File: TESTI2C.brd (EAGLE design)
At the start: 53.3 x 53.3 mm, 20 parts, among them J1 Digital_0_7, J2 Analog, J3 Digital_8_13

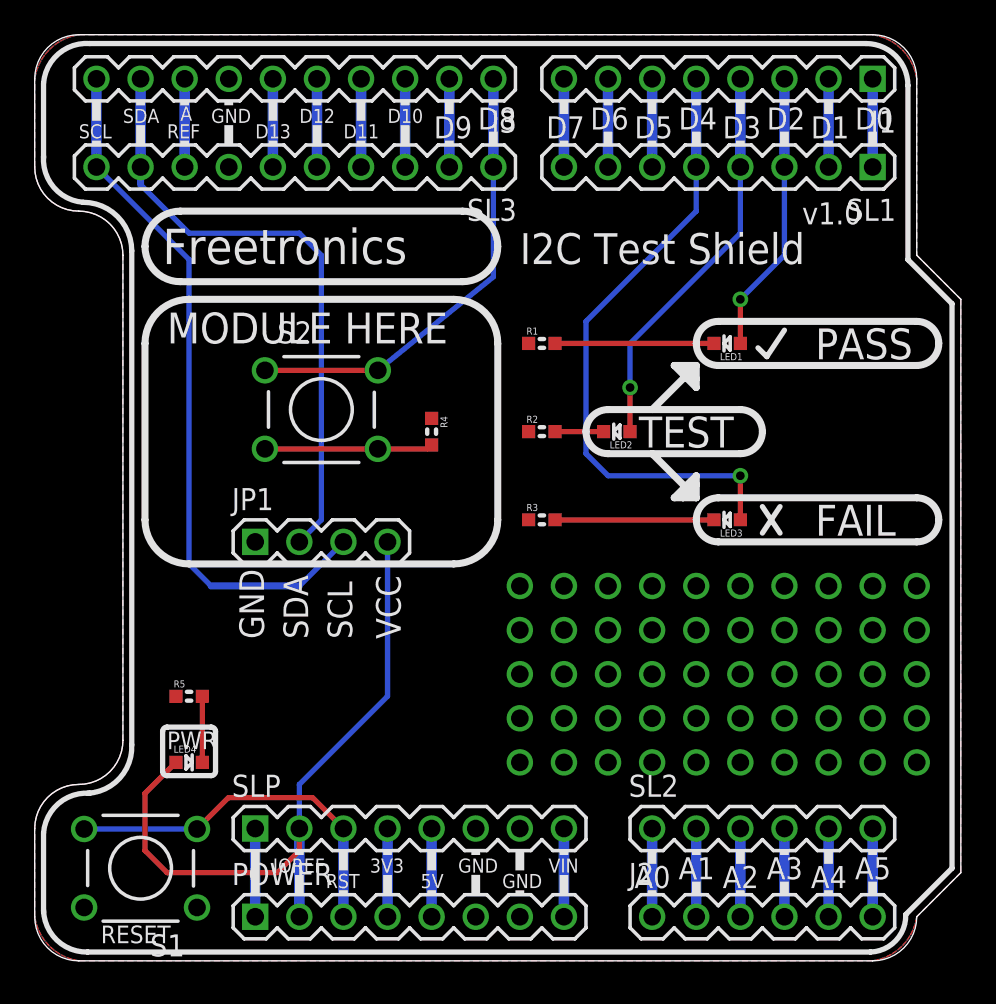
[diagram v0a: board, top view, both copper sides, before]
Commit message: Added piezo
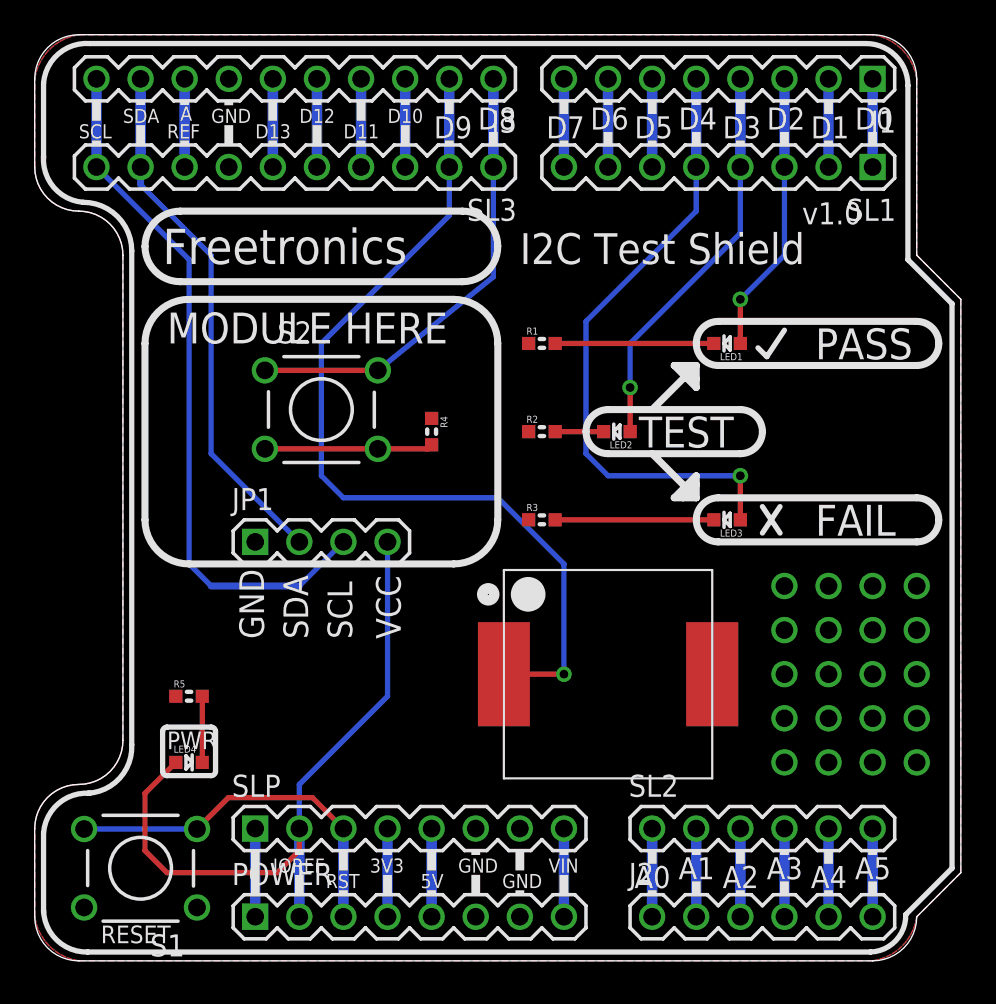
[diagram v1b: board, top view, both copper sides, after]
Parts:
- added PIEZO: BUZZERSMD12X12, freetronics-master-v1:BUZZER-12X12-SMT
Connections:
- net D9: now also PIEZO.2
- net GND: now also PIEZO.1
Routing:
- net D9: track 5.08 -> 51.8 mm, vias 0 -> 1
- net SDA: track 35.2 -> 30.5 mm
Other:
- board text added: "D2: PASS D3: TEST D4: FAIL D8: nDETECT D9: PIEZO"
- board text removed: "D2: PASS D3: TEST D4: FAIL D8: nDETECT"
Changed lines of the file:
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@@
 D3: TEST
 D4: FAIL
-D8: nDETECT</text>
+D8: nDETECT
+D9: PIEZO</text>
 <text x="7.62" y="12.192" size="1.016" layer="21" ratio="15">PWR</text>
 <wire x1="7.62" y1="13.462" x2="7.366" y2="13.208" width="0.3048" layer="21" curve="90"/>
@@
 <element name="LED4" library="freetronics-jon" package="LED-0603" value="BLUE" x="8.89" y="11.43"/>
 <element name="R5" library="freetronics-jon" package="0603" value="1K5 0603" x="8.89" y="15.24"/>
+<element name="PIEZO" library="freetronics-master-v1" package="BUZZER-12X12-SMT" value="BUZZERSMD12X12" x="33.02" y="16.51" rot="R180"/>
 </elements>
 <signals>
@@
 <contactref element="J3" pad="2"/>
 <wire x1="23.876" y1="45.72" x2="23.876" y2="50.8" width="0.6096" layer="16"/>
+<contactref element="PIEZO" pad="2"/>
+<wire x1="27.02" y1="16.51" x2="30.48" y2="16.51" width="0.3048" layer="1"/>
+<via x="30.48" y="16.51" extent="1-16" drill="0.5"/>
+<wire x1="30.48" y1="16.51" x2="30.48" y2="22.86" width="0.3048" layer="16"/>
+<wire x1="30.48" y1="22.86" x2="26.67" y2="26.67" width="0.3048" layer="16"/>
+<wire x1="26.67" y1="26.67" x2="17.78" y2="26.67" width="0.3048" layer="16"/>
+<wire x1="17.78" y1="26.67" x2="16.51" y2="27.94" width="0.3048" layer="16"/>
+<wire x1="16.51" y1="27.94" x2="16.51" y2="35.56" width="0.3048" layer="16"/>
+<wire x1="16.51" y1="35.56" x2="23.876" y2="42.926" width="0.3048" layer="16"/>
+<wire x1="23.876" y1="42.926" x2="23.876" y2="45.72" width="0.3048" layer="16"/>
 </signal>
 <signal name="D8">
@@
 <contactref element="JP1" pad="1"/>
 <contactref element="R5" pad="1"/>
+<contactref element="PIEZO" pad="1"/>
 </signal>
 <signal name="SDA">
@@
 <wire x1="6.096" y1="50.8" x2="6.096" y2="45.72" width="0.6096" layer="16"/>
 <contactref element="JP1" pad="2"/>
-<wire x1="15.24" y1="24.13" x2="16.51" y2="25.4" width="0.3048" layer="16"/>
-<wire x1="16.51" y1="25.4" x2="16.51" y2="40.64" width="0.3048" layer="16"/>
-<wire x1="16.51" y1="40.64" x2="15.24" y2="41.91" width="0.3048" layer="16"/>
-<wire x1="15.24" y1="41.91" x2="8.89" y2="41.91" width="0.3048" layer="16"/>
-<wire x1="8.89" y1="41.91" x2="6.096" y2="44.704" width="0.3048" layer="16"/>
+<wire x1="10.16" y1="40.64" x2="6.096" y2="44.704" width="0.3048" layer="16"/>
 <wire x1="6.096" y1="44.704" x2="6.096" y2="45.72" width="0.4064" layer="16"/>
+<wire x1="15.24" y1="24.13" x2="10.16" y2="29.21" width="0.3048" layer="16"/>
+<wire x1="10.16" y1="29.21" x2="10.16" y2="40.64" width="0.3048" layer="16"/>
 </signal>
 <signal name="SCL">
@@
 <wire x1="9.652" y1="15.24" x2="9.652" y2="11.43" width="0.3048" layer="1"/>
 </signal>
-<signal name="N$5">
-<via x="30.48" y="21.59" extent="1-16" drill="1.016"/>
-</signal>
-<signal name="N$6">
-<via x="33.02" y="21.59" extent="1-16" drill="1.016"/>
-</signal>
-<signal name="N$8">
-<via x="35.56" y="21.59" extent="1-16" drill="1.016"/>
-</signal>
-<signal name="N$9">
-<via x="38.1" y="21.59" extent="1-16" drill="1.016"/>
-</signal>
-<signal name="N$10">
-<via x="40.64" y="21.59" extent="1-16" drill="1.016"/>
-</signal>
 <signal name="N$11">
 <via x="43.18" y="21.59" extent="1-16" drill="1.016"/>
@@
 <via x="43.18" y="19.05" extent="1-16" drill="1.016"/>
 </signal>
-<signal name="N$19">
-<via x="40.64" y="19.05" extent="1-16" drill="1.016"/>
-</signal>
-<signal name="N$20">
-<via x="38.1" y="19.05" extent="1-16" drill="1.016"/>
-</signal>
-<signal name="N$21">
-<via x="35.56" y="19.05" extent="1-16" drill="1.016"/>
-</signal>
-<signal name="N$22">
-<via x="33.02" y="19.05" extent="1-16" drill="1.016"/>
-</signal>
-<signal name="N$23">
-<via x="30.48" y="19.05" extent="1-16" drill="1.016"/>
-</signal>
-<signal name="N$24">
-<via x="30.48" y="16.51" extent="1-16" drill="1.016"/>
-</signal>
-<signal name="N$25">
-<via x="33.02" y="16.51" extent="1-16" drill="1.016"/>
-</signal>
-<signal name="N$26">
-<via x="35.56" y="16.51" extent="1-16" drill="1.016"/>
-</signal>
-<signal name="N$27">
-<via x="38.1" y="16.51" extent="1-16" drill="1.016"/>
-</signal>
-<signal name="N$28">
-<via x="40.64" y="16.51" extent="1-16" drill="1.016"/>
-</signal>
 <signal name="N$29">
 <via x="43.18" y="16.51" extent="1-16" drill="1.016"/>
@@
 <via x="43.18" y="13.97" extent="1-16" drill="1.016"/>
 </signal>
-<signal name="N$37">
-<via x="40.64" y="13.97" extent="1-16" drill="1.016"/>
-</signal>
-<signal name="N$38">
-<via x="38.1" y="13.97" extent="1-16" drill="1.016"/>
-</signal>
-<signal name="N$39">
-<via x="35.56" y="13.97" extent="1-16" drill="1.016"/>
-</signal>
-<signal name="N$40">
-<via x="33.02" y="13.97" extent="1-16" drill="1.016"/>
-</signal>
-<signal name="N$41">
-<via x="30.48" y="13.97" extent="1-16" drill="1.016"/>
-</signal>
-<signal name="N$42">
-<via x="27.94" y="21.59" extent="1-16" drill="1.016"/>
-</signal>
-<signal name="N$43">
-<via x="27.94" y="19.05" extent="1-16" drill="1.016"/>
-</signal>
-<signal name="N$44">
-<via x="27.94" y="16.51" extent="1-16" drill="1.016"/>
-</signal>
-<signal name="N$45">
-<via x="27.94" y="13.97" extent="1-16" drill="1.016"/>
-</signal>
 <signal name="N$46">
 <via x="50.8" y="11.43" extent="1-16" drill="1.016"/>
@@
 <via x="43.18" y="11.43" extent="1-16" drill="1.016"/>
 </signal>
-<signal name="N$50">
-<via x="40.64" y="11.43" extent="1-16" drill="1.016"/>
-</signal>
-<signal name="N$51">
-<via x="38.1" y="11.43" extent="1-16" drill="1.016"/>
-</signal>
-<signal name="N$52">
-<via x="35.56" y="11.43" extent="1-16" drill="1.016"/>
-</signal>
-<signal name="N$53">
-<via x="33.02" y="11.43" extent="1-16" drill="1.016"/>
-</signal>
-<signal name="N$54">
-<via x="30.48" y="11.43" extent="1-16" drill="1.016"/>
-</signal>
-<signal name="N$55">
-<via x="27.94" y="11.43" extent="1-16" drill="1.016"/>
-</signal>
 </signals>

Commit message: Routing and silkscreen for v1.0 release
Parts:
- R1, R2, R3: value 560R 0603 -> 560R
- R4: value 1K 0603 -> 1K
- R5: value 1K5 0603 -> 1K5
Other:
- board text added: "K"
